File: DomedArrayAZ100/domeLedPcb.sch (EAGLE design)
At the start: 117 parts

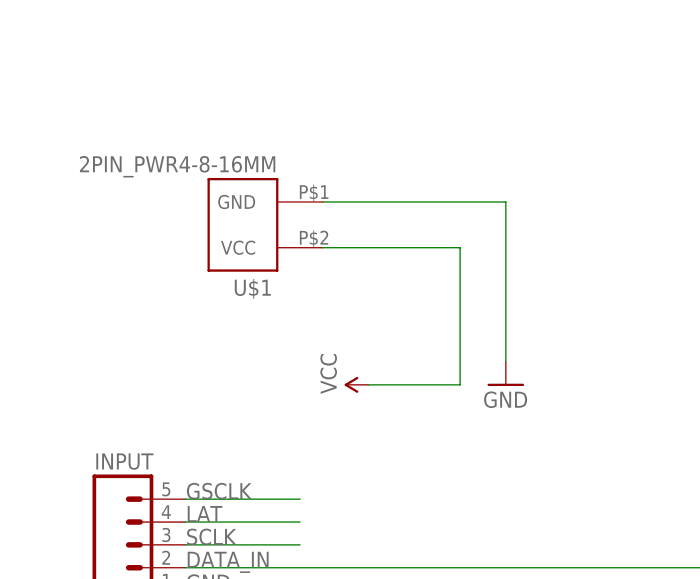
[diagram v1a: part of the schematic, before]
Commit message: new 4P X 8S device and updated DomedArray board
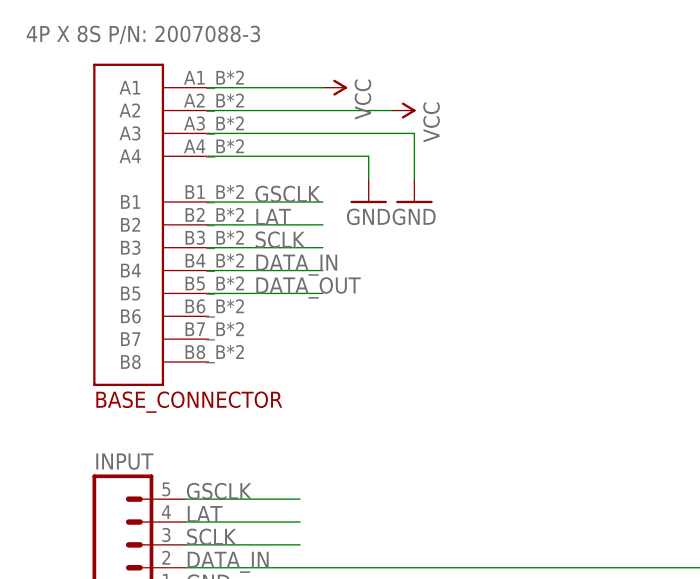
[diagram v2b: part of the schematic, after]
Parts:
- removed U$1: 2PIN_PWR4-8-16MM, WallerLabLib:2PIN_PWR4-8-16MM
- added BASE_CONNECTOR: 4POWER_8SIGNALMATING_BOARD, WallerLabLib:4POWER_8SIGNALMATING_BOARD
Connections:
- net DATA_IN: now also BASE_CONNECTOR.B4
- net DATA_OUT: now also BASE_CONNECTOR.B5
- net GND: now also BASE_CONNECTOR.A3, BASE_CONNECTOR.A4; no longer U$1.GND
- net GSCLK: now also BASE_CONNECTOR.B1
- net LAT: now also BASE_CONNECTOR.B2
- net SCLK: now also BASE_CONNECTOR.B3
- net VCC: now also BASE_CONNECTOR.A1, BASE_CONNECTOR.A2; no longer U$1.VCC
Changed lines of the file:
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@@
 <?xml version="1.0" encoding="utf-8"?>
 <!DOCTYPE eagle SYSTEM "eagle.dtd">
-<eagle version="7.5.0">
+<eagle version="7.4.0">
 <drawing>
 <settings>
@@
 <setting verticaltext="up"/>
 </settings>
-<grid distance="0.1" unitdist="inch" unit="inch" style="lines" multiple="1" display="no" altdistance="0.01" altunitdist="inch" altunit="inch"/>
+<grid distance="0.1" unitdist="inch" unit="inch" style="lines" multiple="1" display="yes" altdistance="0.01" altunitdist="inch" altunit="inch"/>
 <layers>
 <layer number="1" name="Top" color="4" fill="1" visible="no" active="no"/>
@@
 <part name="D96" library="WallerLabLib" deviceset="LED-RGB-CC-THRU" device="CLEAR"/>
 <part name="SUPPLY6" library="SparkFun-Aesthetics" deviceset="VCC" device=""/>
-<part name="SUPPLY7" library="SparkFun-Aesthetics" deviceset="VCC" device=""/>
 <part name="C1" library="SparkFun-Capacitors" deviceset="0.1UF-25V(+80/-20%)(0603)" device="" value="0.1uF"/>
 <part name="C2" library="SparkFun-Capacitors" deviceset="0.1UF-25V(+80/-20%)(0603)" device="" value="0.1uF"/>
@@
 <part name="SUPPLY12" library="SparkFun-Aesthetics" deviceset="VCC" device=""/>
 <part name="SUPPLY13" library="SparkFun-Aesthetics" deviceset="VCC" device=""/>
-<part name="GND1" library="SparkFun-Aesthetics" deviceset="GND" device=""/>
 <part name="INPUT" library="SparkFun-Connectors" deviceset="M05" device="LOCK_LONGPADS" value=" "/>
 <part name="OUTPUT" library="SparkFun-Connectors" deviceset="M05" device="LOCK_LONGPADS" value=" "/>
@@
 <part name="GND14" library="SparkFun-Aesthetics" deviceset="GND" device=""/>
 <part name="GND15" library="SparkFun-Aesthetics" deviceset="GND" device=""/>
-<part name="U$1" library="WallerLabLib" deviceset="2PIN_PWR" device="4-8-16MM" value="2PIN_PWR4-8-16MM"/>
+<part name="BASE_CONNECTOR" library="WallerLabLib" deviceset="4POWER_8SIGNAL" device="MATING_BOARD"/>
+<part name="SUPPLY14" library="SparkFun-Aesthetics" deviceset="VCC" device=""/>
+<part name="SUPPLY15" library="SparkFun-Aesthetics" deviceset="VCC" device=""/>
+<part name="GND16" library="SparkFun-Aesthetics" deviceset="GND" device=""/>
+<part name="GND17" library="SparkFun-Aesthetics" deviceset="GND" device=""/>
 </parts>
 <sheets>
@@
 <instance part="D96" gate="G$1" x="147.32" y="-269.24" rot="R270"/>
 <instance part="SUPPLY6" gate="G$1" x="124.46" y="-215.9"/>
-<instance part="SUPPLY7" gate="G$1" x="-187.96" y="215.9" rot="R90"/>
 <instance part="C1" gate="G$1" x="-27.94" y="22.86" rot="R90"/>
 <instance part="C2" gate="G$1" x="269.24" y="-139.7" rot="R90"/>
@@
 <instance part="SUPPLY12" gate="G$1" x="-17.78" y="17.78" rot="R180"/>
 <instance part="SUPPLY13" gate="G$1" x="276.86" y="35.56" rot="R180"/>
-<instance part="GND1" gate="1" x="-172.72" y="215.9"/>
 <instance part="INPUT" gate="G$1" x="-215.9" y="198.12"/>
 <instance part="OUTPUT" gate="G$1" x="-215.9" y="175.26"/>
@@
 <instance part="GND14" gate="1" x="256.54" y="-142.24"/>
 <instance part="GND15" gate="1" x="256.54" y="35.56"/>
-<instance part="U$1" gate="G$1" x="-200.66" y="233.68" rot="R180"/>
+<instance part="BASE_CONNECTOR" gate="G$1" x="-215.9" y="233.68"/>
+<instance part="SUPPLY14" gate="G$1" x="-193.04" y="248.92" rot="R270"/>
+<instance part="SUPPLY15" gate="G$1" x="-185.42" y="246.38" rot="R270"/>
+<instance part="GND16" gate="1" x="-182.88" y="236.22"/>
+<instance part="GND17" gate="1" x="-187.96" y="236.22"/>
 </instances>
 <busses>
@@
 </segment>
 <segment>
-<wire x1="-193.04" y1="231.14" x2="-177.8" y2="231.14" width="0.1524" layer="91"/>
-<wire x1="-177.8" y1="215.9" x2="-177.8" y2="231.14" width="0.1524" layer="91"/>
-<pinref part="U$1" gate="G$1" pin="VCC"/>
-<pinref part="SUPPLY7" gate="G$1" pin="VCC"/>
-<wire x1="-177.8" y1="215.9" x2="-187.96" y2="215.9" width="0.1524" layer="91"/>
+<pinref part="BASE_CONNECTOR" gate="G$1" pin="A1"/>
+<wire x1="-205.74" y1="248.92" x2="-193.04" y2="248.92" width="0.1524" layer="91"/>
+<pinref part="SUPPLY14" gate="G$1" pin="VCC"/>
+</segment>
+<segment>
+<pinref part="BASE_CONNECTOR" gate="G$1" pin="A2"/>
+<wire x1="-205.74" y1="246.38" x2="-185.42" y2="246.38" width="0.1524" layer="91"/>
+<pinref part="SUPPLY15" gate="G$1" pin="VCC"/>
 </segment>
 </net>
@@
 <label x="269.24" y="-208.28" size="1.778" layer="95" rot="R90"/>
 </segment>
+<segment>
+<pinref part="BASE_CONNECTOR" gate="G$1" pin="B3"/>
+<wire x1="-205.74" y1="231.14" x2="-193.04" y2="231.14" width="0.1524" layer="91"/>
+<label x="-200.66" y="231.14" size="1.778" layer="95"/>
+</segment>
 </net>
 <net name="N$283" class="0">
@@
 <label x="-22.86" y="-35.56" size="1.778" layer="95" rot="R90"/>
 </segment>
+<segment>
+<pinref part="BASE_CONNECTOR" gate="G$1" pin="B2"/>
+<wire x1="-205.74" y1="233.68" x2="-193.04" y2="233.68" width="0.1524" layer="91"/>
+<label x="-200.66" y="233.68" size="1.778" layer="95"/>
+</segment>
 </net>
 <net name="N$285" class="0">
@@
 <label x="-20.32" y="-35.56" size="1.778" layer="95" rot="R90"/>
 </segment>
+<segment>
+<pinref part="BASE_CONNECTOR" gate="G$1" pin="B1"/>
+<wire x1="-205.74" y1="236.22" x2="-193.04" y2="236.22" width="0.1524" layer="91"/>
+<label x="-200.66" y="236.22" size="1.778" layer="95"/>
+</segment>
 </net>
 <net name="GND" class="0">
@@
 </segment>
 <segment>
-<pinref part="GND1" gate="1" pin="GND"/>
-<wire x1="-193.04" y1="236.22" x2="-172.72" y2="236.22" width="0.1524" layer="91"/>
-<wire x1="-172.72" y1="236.22" x2="-172.72" y2="218.44" width="0.1524" layer="91"/>
-<pinref part="U$1" gate="G$1" pin="GND"/>
-</segment>
-<segment>
 <pinref part="INPUT" gate="G$1" pin="1"/>
 <pinref part="GND8" gate="1" pin="GND"/>
@@
 <wire x1="-43.18" y1="147.32" x2="-40.64" y2="147.32" width="0.1524" layer="91"/>
 </segment>
+<segment>
+<pinref part="BASE_CONNECTOR" gate="G$1" pin="A3"/>
+<wire x1="-205.74" y1="243.84" x2="-182.88" y2="243.84" width="0.1524" layer="91"/>
+<pinref part="GND16" gate="1" pin="GND"/>
+<wire x1="-182.88" y1="243.84" x2="-182.88" y2="238.76" width="0.1524" layer="91"/>
+</segment>
+<segment>
+<pinref part="BASE_CONNECTOR" gate="G$1" pin="A4"/>
+<wire x1="-205.74" y1="241.3" x2="-187.96" y2="241.3" width="0.1524" layer="91"/>
+<pinref part="GND17" gate="1" pin="GND"/>
+<wire x1="-187.96" y1="241.3" x2="-187.96" y2="238.76" width="0.1524" layer="91"/>
+</segment>
 </net>
 <net name="N$288" class="0">
@@
 <junction x="-27.94" y="142.24"/>
 </segment>
+<segment>
+<pinref part="BASE_CONNECTOR" gate="G$1" pin="B5"/>
+<wire x1="-205.74" y1="226.06" x2="-193.04" y2="226.06" width="0.1524" layer="91"/>
+<label x="-200.66" y="226.06" size="1.778" layer="95"/>
+</segment>
 </net>
 <net name="DATA_IN" class="0">
@@
 <label x="-208.28" y="195.58" size="1.778" layer="95"/>
 </segment>
+<segment>
+<pinref part="BASE_CONNECTOR" gate="G$1" pin="B4"/>
+<wire x1="-205.74" y1="228.6" x2="-193.04" y2="228.6" width="0.1524" layer="91"/>
+<label x="-200.66" y="228.6" size="1.778" layer="95"/>
+</segment>
 </net>
